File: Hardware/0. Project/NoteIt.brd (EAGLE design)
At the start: 50 x 50 mm, 61 parts, among them SW1 KY-040

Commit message: WIP
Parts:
- C1, C10, C11, C15, C16, C19, C24, C25, C3, C39, C4, C7, C8, C9: device rcl:C0603 -> My-RLC:C0603
- C14: device rcl:C0805 -> My-RLC:C0603
- R1, R10, R11, R12, R13, R14, R15, R17, R18, R2, R22, R3, R4, R41, R42, R5, R9: device rcl:R0603 -> My-RLC:R0603
- moved C3 374.0 mm to (-0.76, -306.7)
- moved C25 363.1 mm to (-0.76, -332.1)
- moved C4 356.2 mm to (-0.76, -294.0)
- moved C14 349.6 mm to (-0.76, -319.4)
- moved C11 301.7 mm to (-0.76, -281.3)
- moved C10 294.1 mm to (-0.76, -268.6)
- moved C24 294.0 mm to (-0.76, -217.8)
- moved C7 286.5 mm to (-0.76, -255.9)
- moved C1 282.7 mm to (-0.76, -243.2)
- moved C39 248.9 mm to (-0.76, -230.5)
- moved R5 241.7 mm to (-0.76, -179.7)
- moved C9 230.6 mm to (-0.76, -205.1)
- moved R14 227.6 mm to (-0.76, -167.0)
- moved R17 220.6 mm to (-0.76, -154.3)
- moved C8 208.8 mm to (-0.76, -192.4)
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
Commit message: SCH vs BRD conflicts fix
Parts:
- CN1: value (none) -> USB 3.2 Gen 2 Type C Receptacle; device Micro SD:MICROSD-PUSH-OUT -> USB C CONNECOTR:GCT_USB4080-03-A_REVA
- CN3: value (none) -> Micro-SD Card; device USB C CONNECOTR:GCT_USB4080-03-A_REVA -> Micro SD:MICROSD-PUSH-OUT
- U2: value (none) -> GL823K
- moved CN3 384.8 mm to (-67.3, -325.1), turned to 0 degrees
- moved U2 365.1 mm to (-43.2, -336.6), flipped to the top, turned to 0 degrees
- moved CN1 363.2 mm to (-53.3, -331.5), flipped to the top, turned to 0 degrees
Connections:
- net !SDCARD_CARD_DETECT!: now also CN3.9; no longer CN1.9
- net 0V: now also CN1.A1, CN1.A12, CN1.B1, CN1.B12, CN3.6, CN3.G1, CN3.G2, CN3.G3, CN3.G4; no longer CN1.6, CN1.G1, CN1.G2, CN1.G3, CN1.G4, CN3.A1, CN3.A12, CN3.B1, CN3.B12
- net 3.3V: now also CN3.4; no longer CN1.4
- net N$10: now also CN1.G1, CN1.G2, CN1.G3, CN1.G4; no longer CN3.G1, CN3.G2, CN3.G3, CN3.G4
- net N$15: now also CN3.3; no longer CN1.3
- net N$16: now also CN3.7; no longer CN1.7
- net N$2: now also CN3.5; no longer CN1.5
- net N$20: now also CN3.8; no longer CN1.8
- net N$21: now also CN1.B5; no longer CN3.B5
- net N$6: now also CN1.A5; no longer CN3.A5
- net N$7: now also CN3.1; no longer CN1.1
- net N$8: now also CN3.2; no longer CN1.2
- net USB_N: now also CN1.A7, CN1.B6, U2.15; no longer CN3.A7, CN3.B7, U2.16
- net USB_P: now also CN1.A6, CN1.B7, U2.16; no longer CN3.A6, CN3.B6, U2.15
- net VUSB: now also CN1.A4, CN1.A9, CN1.B4, CN1.B9; no longer CN3.A4, CN3.A9, CN3.B4, CN3.B9

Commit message: PCB design WIP
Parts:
- removed G1: (no value), battery:CH291-1220LF
- added BAT1: CR1220, SamacSys_Parts:1072
- DS1: value (none) -> DISPLAY-OLED-128X64
- moved C25 394.3 mm to (95.8, 50.2)
- moved U2 388.9 mm to (40.6, 43.2)
- moved C14 380.4 mm to (89.4, 50.2)
- moved CN3 359.2 mm to (8.38, 26.0), flipped to the bottom, turned to 90 degrees
- moved CN1 352.2 mm to (43.9, 6.99)
- moved C10 318.2 mm to (81.8, 38.7)
- moved C11 318.2 mm to (81.8, 26.0)
- moved C7 318.2 mm to (81.8, 51.4)
- moved C3 318.2 mm to (81.8, 0.64)
- moved C4 318.2 mm to (81.8, 13.3)
- moved C1 283.9 mm to (89.4, 26.0)
- moved C39 283.9 mm to (89.4, 38.7)
- moved C24 229.3 mm to (72.9, -0.64)
- moved C8 229.3 mm to (72.9, 24.8)
- moved R5 229.3 mm to (72.9, 37.5)
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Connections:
- net 0V: now also BAT1.-; no longer G1.-
- net N$22: now also BAT1.+; no longer G1.+

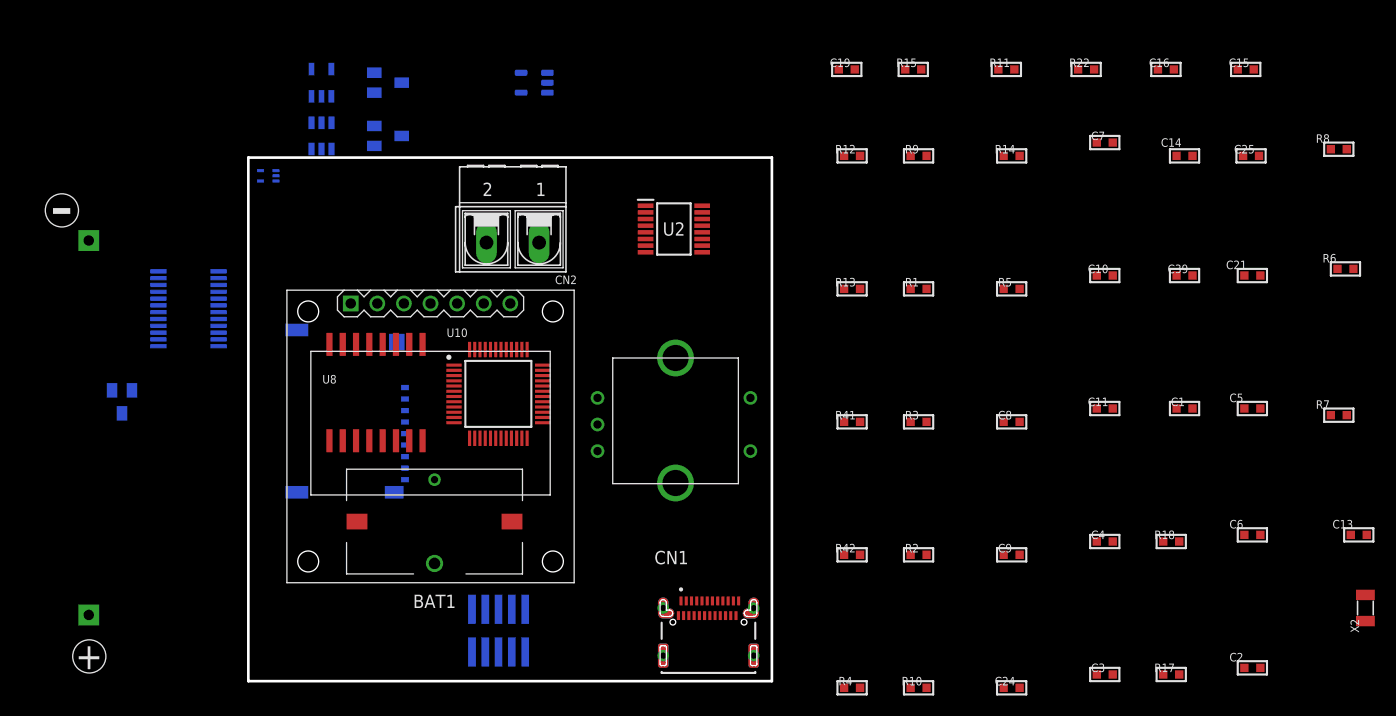
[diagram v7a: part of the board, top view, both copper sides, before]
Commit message: Standardization footprints from the same package type
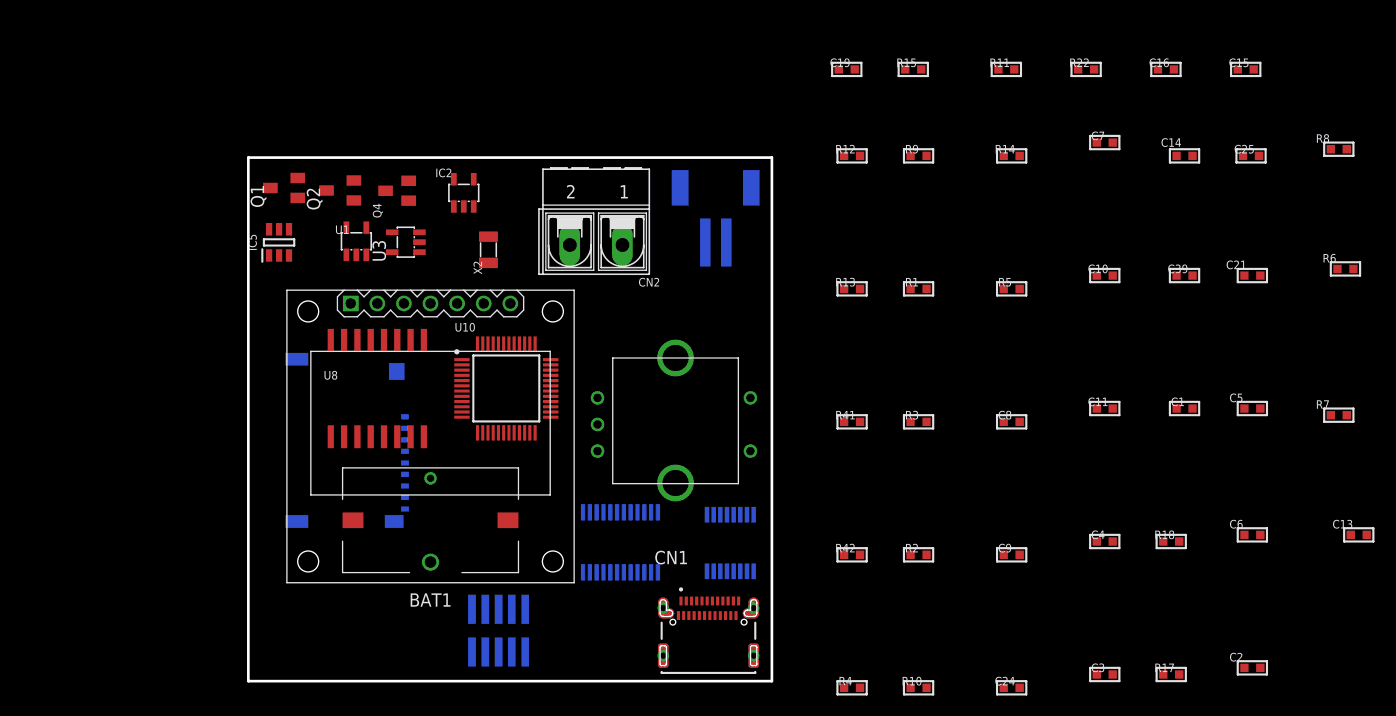
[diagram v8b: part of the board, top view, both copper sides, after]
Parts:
- removed BT2: LiPO, Battery:+
- removed Q3: (no value), SI2374DS:SOT-23(TO-236)
- removed U5: (no value), TLV75530PDBVR:SOT95P280X145-5N
- added CN6: Lithium Ion Polymer, Battery:JST-PH-2-SMT-RA
- added Q1: SI2374DS, SI2374DS:SOT-23(TO-236)
- added U3: TLV75530PDBVR, TLV75530PDBVR:SOT23-5L
- CN4: value (none) -> FTSH-105-01-L-DV-K-TR
- IC5: value (none) -> S-8261ACMMD-G4MT2U
- Q2: value (none) -> SI2374DS
- U1: value (none) -> SN74AHC1G125DBV; device SN74AHC1G125DRLR:SOT-553 -> SN74AHC1G125DRLR:SOT23-5
- U4: value (none) -> TS3A27518EPWR
- U8: value (none) -> DS3231/SO
- moved X2 90.5 mm to (22.9, 41.2)
- moved U4 46.9 mm to (35.5, 13.3), turned to 270 degrees
- moved Q4 33.1 mm to (14.2, 46.8), flipped to the top, turned to 90 degrees
- moved U2 30.5 mm to (46.0, 13.2), flipped to the bottom, turned to 270 degrees
- moved IC2 17.2 mm to (20.6, 46.6), flipped to the top
- moved Q2 11.3 mm to (8.77, 46.9), flipped to the top
- moved IC5 10.9 mm to (2.94, 41.9), flipped to the top
- moved U1 10.5 mm to (10.3, 42.0), flipped to the top
- moved CN2 7.96 mm to (33.2, 41.7)
- moved CN3 2.79 mm to (8.38, 23.2)
- moved U10 0.92 mm to (24.6, 28.0)
- moved BAT1 0.40 mm to (17.4, 15.4)
- moved U8 0.40 mm to (12.3, 27.9)
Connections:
- net 0V: now also U3.2; no longer U5.2
- net 3.3V: now also U3.5; no longer U5.5
- net N$1: now also Q1.1; no longer Q3.1
- net N$3: now also Q1.3; no longer Q3.3
- net N$32: now also CN6.2, Q1.2; no longer BT2.GND, Q3.2
- net N$33: now also CN6.1, U3.1, U3.3; no longer BT2.VDD, U5.1, U5.3
